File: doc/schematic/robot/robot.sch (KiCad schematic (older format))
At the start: 10 parts

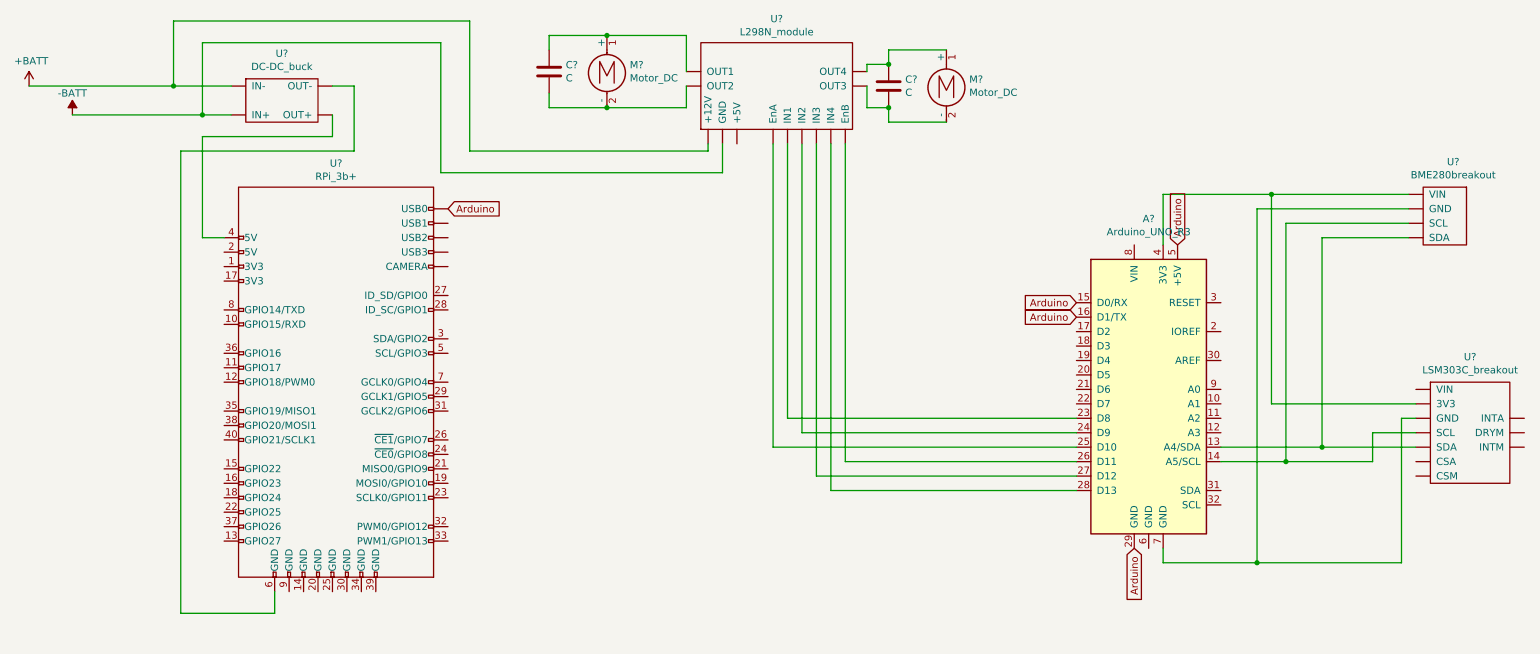
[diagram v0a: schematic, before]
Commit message: Robot GUI for changing HSV inRange parameters
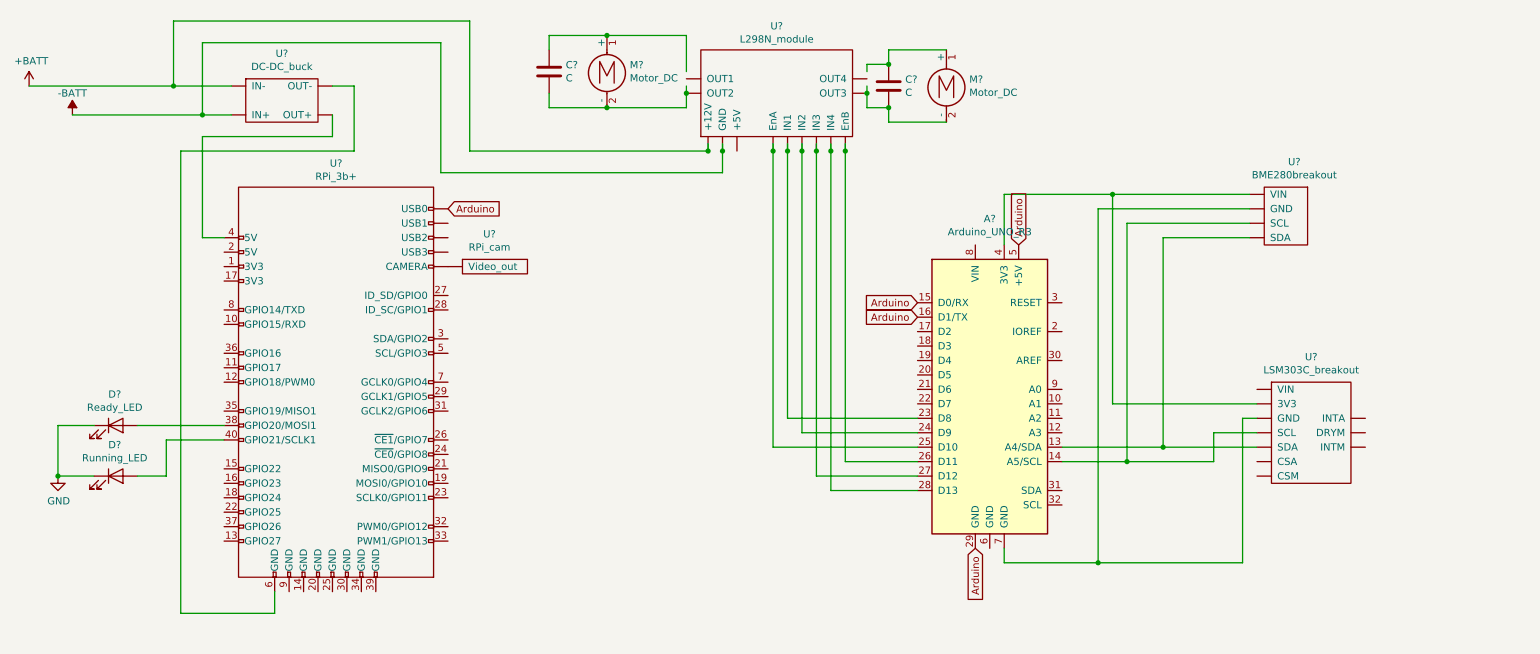
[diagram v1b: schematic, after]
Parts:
- added D?: Ready_LED, symbol Device:LED
- added D?: Running_LED, symbol Device:LED
- added U?: RPi_cam, symbol robot:RPi_cam
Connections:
- net labels added: GND
- wire segments 74 -> 90
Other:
- moved on the sheet: A?, U?
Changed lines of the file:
@@
 EESchema Schematic File Version 4
+LIBS:robot-cache
 EELAYER 29 0
 EELAYER END
@@
 L MCU_Module:Arduino_UNO_R3 A?
 U 1 1 5CBB77F7
-P 8400 3600
-F 0 "A?" H 8400 4781 50  0000 C CNN
-F 1 "Arduino_UNO_R3" H 8400 4690 50  0000 C CNN
-F 2 "Module:Arduino_UNO_R3" H 8550 2550 50  0001 L CNN
-F 3 "https://www.arduino.cc/en/Main/arduinoBoardUno" H 8200 4650 50  0001 C CNN
-	1    8400 3600
+P 7300 3600
+F 0 "A?" H 7300 4781 50  0000 C CNN
+F 1 "Arduino_UNO_R3" H 7300 4690 50  0000 C CNN
+F 2 "Module:Arduino_UNO_R3" H 7450 2550 50  0001 L CNN
+F 3 "https://www.arduino.cc/en/Main/arduinoBoardUno" H 7100 4650 50  0001 C CNN
+	1    7300 3600
 	1    0    0    -1
 $EndComp
@@
 L robot:BME280breakout U?
 U 1 1 5CBD2A13
-P 10450 2150
-F 0 "U?" H 10508 2275 50  0000 C CNN
-F 1 "BME280breakout" H 10508 2184 50  0000 C CNN
-F 2 "" H 10450 2150 50  0001 C CNN
-F 3 "" H 10450 2150 50  0001 C CNN
-	1    10450 2150
+P 9350 2150
+F 0 "U?" H 9408 2275 50  0000 C CNN
+F 1 "BME280breakout" H 9408 2184 50  0000 C CNN
+F 2 "" H 9350 2150 50  0001 C CNN
+F 3 "" H 9350 2150 50  0001 C CNN
+	1    9350 2150
 	1    0    0    -1
 $EndComp
@@
 L robot:LSM303C_breakout U?
 U 1 1 5CBD3076
-P 10650 3500
-F 0 "U?" H 10625 3625 50  0000 C CNN
-F 1 "LSM303C_breakout" H 10625 3534 50  0000 C CNN
-F 2 "" H 10650 3500 50  0001 C CNN
-F 3 "" H 10650 3500 50  0001 C CNN
-	1    10650 3500
+P 9550 3500
+F 0 "U?" H 9525 3625 50  0000 C CNN
+F 1 "LSM303C_breakout" H 9525 3534 50  0000 C CNN
+F 2 "" H 9550 3500 50  0001 C CNN
+F 3 "" H 9550 3500 50  0001 C CNN
+	1    9550 3500
 	1    0    0    -1
 $EndComp
@@
 Text GLabel 3550 2350 2    50   Input ~ 0
 Arduino
-Text GLabel 8300 4700 3    50   Input ~ 0
+Text GLabel 7200 4700 3    50   Input ~ 0
 Arduino
-Text GLabel 7900 3100 0    50   Input ~ 0
+Text GLabel 6800 3100 0    50   Input ~ 0
 Arduino
-Text GLabel 7900 3000 0    50   Input ~ 0
+Text GLabel 6800 3000 0    50   Input ~ 0
 Arduino
-Text GLabel 8600 2600 1    50   Input ~ 0
+Text GLabel 7500 2600 1    50   Input ~ 0
 Arduino
 $Comp
@@
 L robot:L298N_module U?
 U 1 1 5CBE7604
-P 5600 1150
-F 0 "U?" H 5825 1265 50  0000 C CNN
-F 1 "L298N_module" H 5825 1174 50  0000 C CNN
-F 2 "" H 5600 1150 50  0001 C CNN
-F 3 "" H 5600 1150 50  0001 C CNN
-	1    5600 1150
+P 5600 1200
+F 0 "U?" H 5825 1315 50  0000 C CNN
+F 1 "L298N_module" H 5825 1224 50  0000 C CNN
+F 2 "" H 5600 1200 50  0001 C CNN
+F 3 "" H 5600 1200 50  0001 C CNN
+	1    5600 1200
 	1    0    0    -1
 $EndComp
@@
 	2350 5150 2350 5000
 Wire Wire Line
-	8500 2600 8500 2250
-Wire Wire Line
-	8500 2250 9250 2250
-Wire Wire Line
-	9250 2250 9250 3700
-Wire Wire Line
-	9250 3700 10250 3700
-Wire Wire Line
-	8900 4000 9600 4000
-Wire Wire Line
-	9600 2550 9600 4000
-Connection ~ 9600 4000
-Wire Wire Line
-	9600 4000 10250 4000
-Wire Wire Line
-	8900 4100 9350 4100
-Wire Wire Line
-	9950 4100 9950 3900
-Wire Wire Line
-	9950 3900 10250 3900
-Wire Wire Line
-	9350 4100 9350 2450
-Connection ~ 9350 4100
-Wire Wire Line
-	9350 4100 9950 4100
-Wire Wire Line
-	8500 4700 8500 4800
-Wire Wire Line
-	8500 4800 9150 4800
-Wire Wire Line
-	9150 4800 9150 2350
-Wire Wire Line
-	9150 4800 10150 4800
-Wire Wire Line
-	10150 4800 10150 3800
-Wire Wire Line
-	10150 3800 10250 3800
-Connection ~ 9150 4800
+	7400 2600 7400 2250
+Wire Wire Line
+	7400 2250 8150 2250
+Wire Wire Line
+	8150 2250 8150 3700
+Wire Wire Line
+	8150 3700 9150 3700
+Wire Wire Line
+	7800 4000 8500 4000
+Wire Wire Line
+	8500 2550 8500 4000
+Connection ~ 8500 4000
+Wire Wire Line
+	8500 4000 9150 4000
+Wire Wire Line
+	7800 4100 8250 4100
+Wire Wire Line
+	8850 4100 8850 3900
+Wire Wire Line
+	8850 3900 9150 3900
+Wire Wire Line
+	8250 4100 8250 2450
+Connection ~ 8250 4100
+Wire Wire Line
+	8250 4100 8850 4100
+Wire Wire Line
+	7400 4700 7400 4800
+Wire Wire Line
+	7400 4800 8050 4800
+Wire Wire Line
+	8050 4800 8050 2350
+Wire Wire Line
+	8050 4800 9050 4800
+Wire Wire Line
+	9050 4800 9050 3800
+Wire Wire Line
+	9050 3800 9150 3800
+Connection ~ 8050 4800
 Wire Wire Line
 	6450 1400 6450 1350
@@
 Connection ~ 6600 1350
 Wire Wire Line
-	6450 1500 6450 1650
+	6450 1500 6450 1550
 Wire Wire Line
 	6450 1650 6600 1650
@@
 Connection ~ 4650 1150
 Wire Wire Line
-	5200 1500 5200 1650
+	5200 1500 5200 1550
 Wire Wire Line
 	5200 1650 4650 1650
@@
 	950  1700 1850 1700
 Wire Wire Line
-	9250 2250 10200 2250
-Connection ~ 9250 2250
-Wire Wire Line
-	9150 2350 10200 2350
-Wire Wire Line
-	9350 2450 10200 2450
-Wire Wire Line
-	9600 2550 10200 2550
-Wire Wire Line
-	7900 4000 5800 4000
-Wire Wire Line
-	5800 4000 5800 1900
-Wire Wire Line
-	7900 4100 6300 4100
-Wire Wire Line
-	6300 4100 6300 1900
-Wire Wire Line
-	7900 3800 5900 3800
-Wire Wire Line
-	5900 3800 5900 1900
-Wire Wire Line
-	7900 3900 6000 3900
-Wire Wire Line
-	6000 3900 6000 1900
-Wire Wire Line
-	7900 4200 6100 4200
-Wire Wire Line
-	6100 4200 6100 1900
-Wire Wire Line
-	7900 4300 6200 4300
-Wire Wire Line
-	6200 4300 6200 1900
+	8150 2250 9100 2250
+Connection ~ 8150 2250
+Wire Wire Line
+	8050 2350 9100 2350
+Wire Wire Line
+	8250 2450 9100 2450
+Wire Wire Line
+	8500 2550 9100 2550
+Wire Wire Line
+	6800 4000 5800 4000
+Wire Wire Line
+	5800 4000 5800 1950
+Wire Wire Line
+	6800 4100 6300 4100
+Wire Wire Line
+	6300 4100 6300 1950
+Wire Wire Line
+	6800 3800 5900 3800
+Wire Wire Line
+	5900 3800 5900 1950
+Wire Wire Line
+	6800 3900 6000 3900
+Wire Wire Line
+	6000 3900 6000 1950
+Wire Wire Line
+	6800 4200 6100 4200
+Wire Wire Line
+	6100 4200 6100 1950
+Wire Wire Line
+	6800 4300 6200 4300
+Wire Wire Line
+	6200 4300 6200 1950
 Wire Wire Line
 	1650 1500 1650 1050
@@
 	3500 2100 5450 2100
 Wire Wire Line
-	5450 2100 5450 1900
+	5450 2100 5450 1950
 Connection ~ 1850 1700
 Wire Wire Line
 	1850 1700 2050 1700
+$Comp
+L Device:LED D?
+U 1 1 5CCB8547
+P 1250 3850
+F 0 "D?" H 1243 4066 50  0000 C CNN
+F 1 "Ready_LED" H 1243 3975 50  0000 C CNN
+F 2 "" H 1250 3850 50  0001 C CNN
+F 3 "~" H 1250 3850 50  0001 C CNN
+	1    1250 3850
+	1    0    0    -1
+$EndComp
+$Comp
+L Device:LED D?
+U 1 1 5CCBBC55
+P 1250 4200
+F 0 "D?" H 1243 4416 50  0000 C CNN
+F 1 "Running_LED" H 1243 4325 50  0000 C CNN
+F 2 "" H 1250 4200 50  0001 C CNN
+F 3 "~" H 1250 4200 50  0001 C CNN
+	1    1250 4200
+	1    0    0    -1
+$EndComp
+Wire Wire Line
+	1400 3850 2000 3850
+Wire Wire Line
+	2000 3950 1600 3950
+Wire Wire Line
+	1600 3950 1600 4200
+Wire Wire Line
+	1600 4200 1400 4200
+$Comp
+L power:GND #PWR?
+U 1 1 5CCC0411
+P 850 4200
+F 0 "#PWR?" H 850 3950 50  0001 C CNN
+F 1 "GND" H 855 4027 50  0000 C CNN
+F 2 "" H 850 4200 50  0001 C CNN
+F 3 "" H 850 4200 50  0001 C CNN
+	1    850  4200
+	1    0    0    -1
+$EndComp
+Wire Wire Line
+	1100 3850 850  3850
+Wire Wire Line
+	850  3850 850  4200
+Wire Wire Line
+	1100 4200 850  4200
+Connection ~ 850  4200
+Connection ~ 5200 1550
+Wire Wire Line
+	5200 1550 5200 1650
+Connection ~ 5350 1950
+Connection ~ 5450 1950
+Wire Wire Line
+	5450 1950 5450 1900
+Connection ~ 5800 1950
+Wire Wire Line
+	5800 1950 5800 1900
+Connection ~ 5900 1950
+Wire Wire Line
+	5900 1950 5900 1900
+Connection ~ 6000 1950
+Wire Wire Line
+	6000 1950 6000 1900
+Connection ~ 6100 1950
+Wire Wire Line
+	6100 1950 6100 1900
+Connection ~ 6200 1950
+Wire Wire Line
+	6200 1950 6200 1900
+Connection ~ 6300 1950
+Wire Wire Line
+	6300 1950 6300 1900
+Connection ~ 6450 1550
+Wire Wire Line
+	6450 1550 6450 1650
+$Comp
+L robot:RPi_cam U?
+U 1 1 5CCCFA59
+P 3900 2650
+F 0 "U?" H 3837 2775 50  0000 C CNN
+F 1 "RPi_cam" H 3837 2684 50  0000 C CNN
+F 2 "" H 3900 2650 50  0001 C CNN
+F 3 "" H 3900 2650 50  0001 C CNN
+	1    3900 2650
+	1    0    0    -1
+$EndComp
 $EndSCHEMATC

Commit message: PID tuning, added GUI to circle recognition, fixed remote control speed change bug
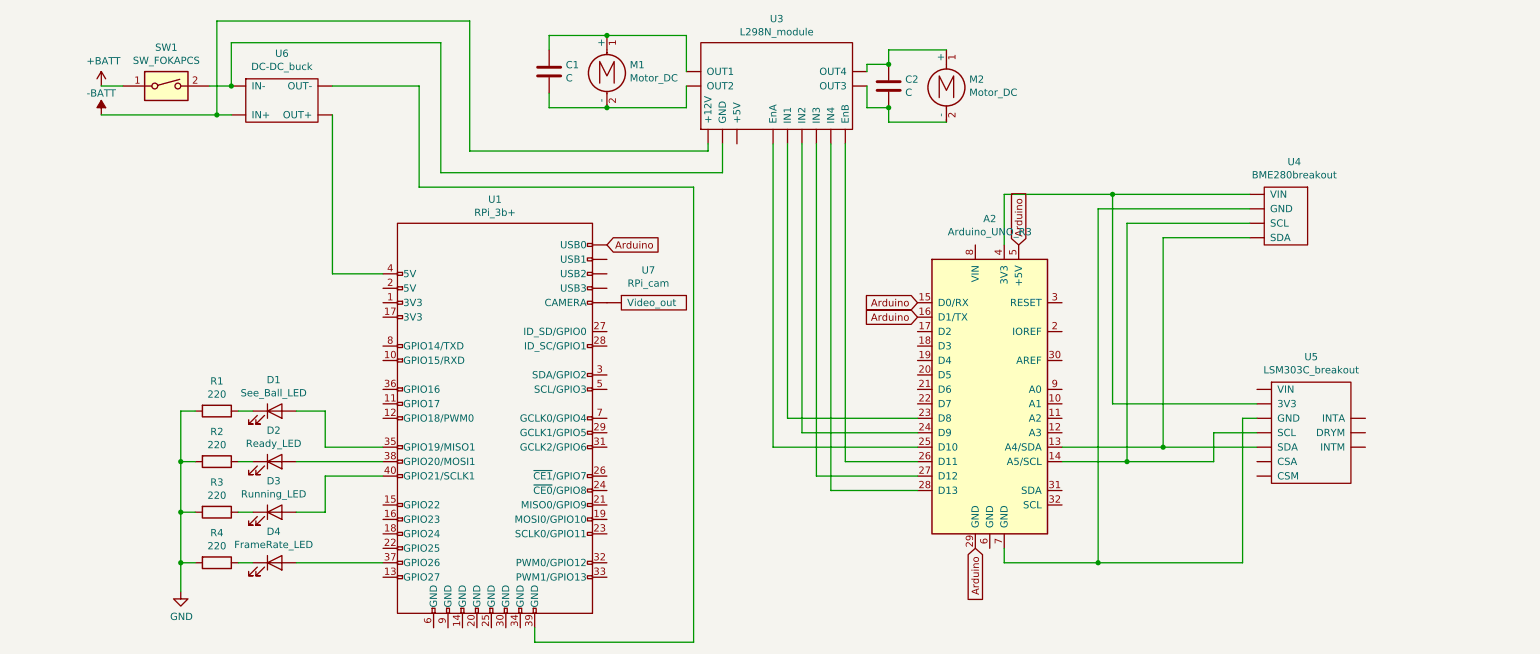
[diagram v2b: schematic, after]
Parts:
- added D1: See_Ball_LED, symbol Device:LED
- added D4: FrameRate_LED, symbol Device:LED
- added R1, R2, R3, R4: 220, symbol Device:R
- added SW1: SW_FOKAPCS, symbol Switch:SW_DIP_x01
- gave numbers to parts that had none: 13
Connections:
- wire segments 90 -> 92
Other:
- moved on the sheet: D2, D3, U1, U3, U7
